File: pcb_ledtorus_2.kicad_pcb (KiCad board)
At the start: 4 copper layers, 149 x 149 mm, 279 parts, among them P1 CONN_02X04, P2 CONN_6, P3 MICRO-SD, P4 CONN_2, P5 KNUSB, P6 CONN_12, U1 STM32F46X_LQFP176, U10 TLC5955, U11 TLC5955, U12 TLC5955, U13 TLC5955, U14 TLC5955, U15 TLC5955, U2 US4881_HALL, U3 LP38691, U4 TLC5955, U5 TLC5955, U6 TLC5955, U7 TLC5955, U8 TLC5955, U9 TLC5955, X1 MA-505

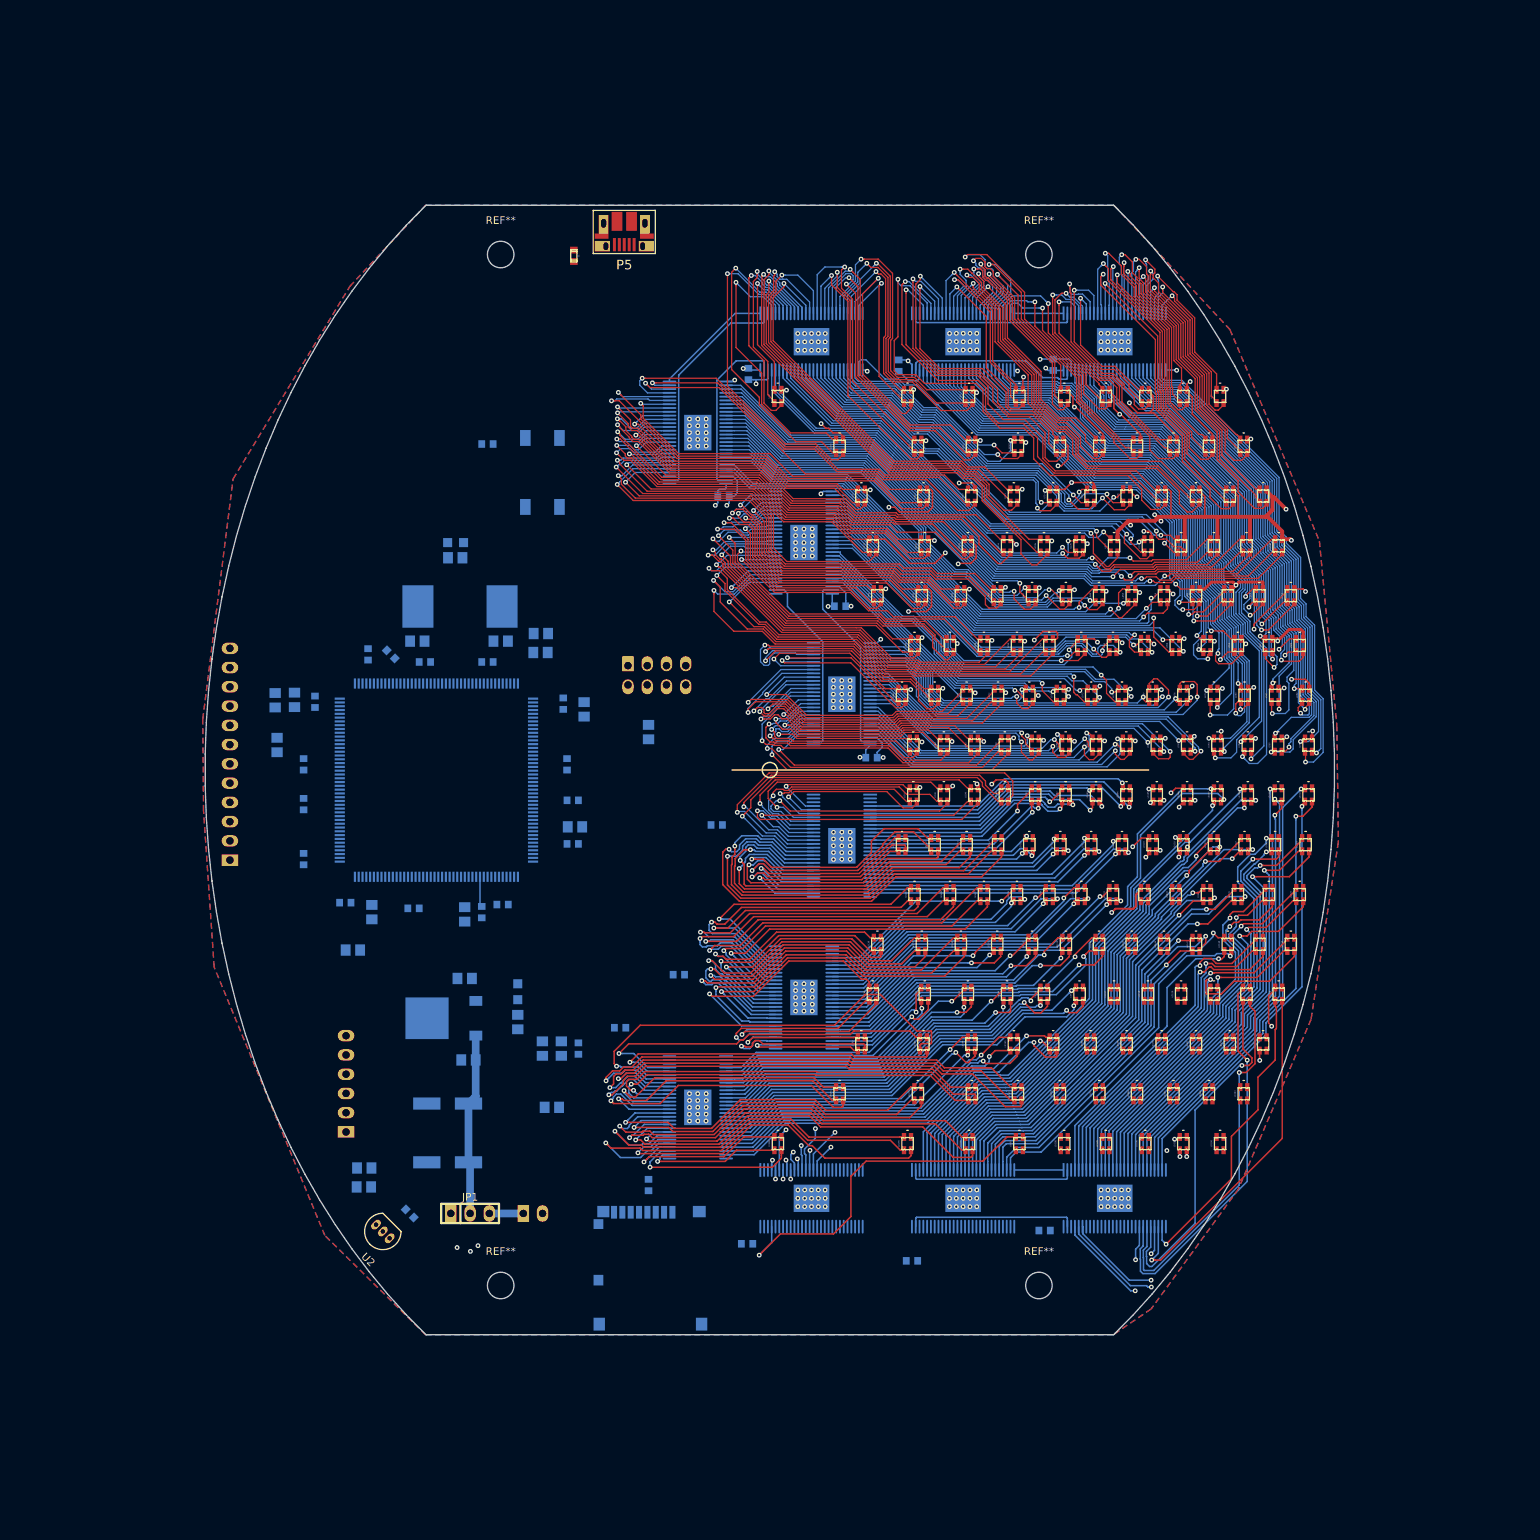
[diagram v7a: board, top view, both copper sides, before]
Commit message: Some preliminary routing of signals between TLCs and MCU.
Mostly to check that everything looks reasonably possible.
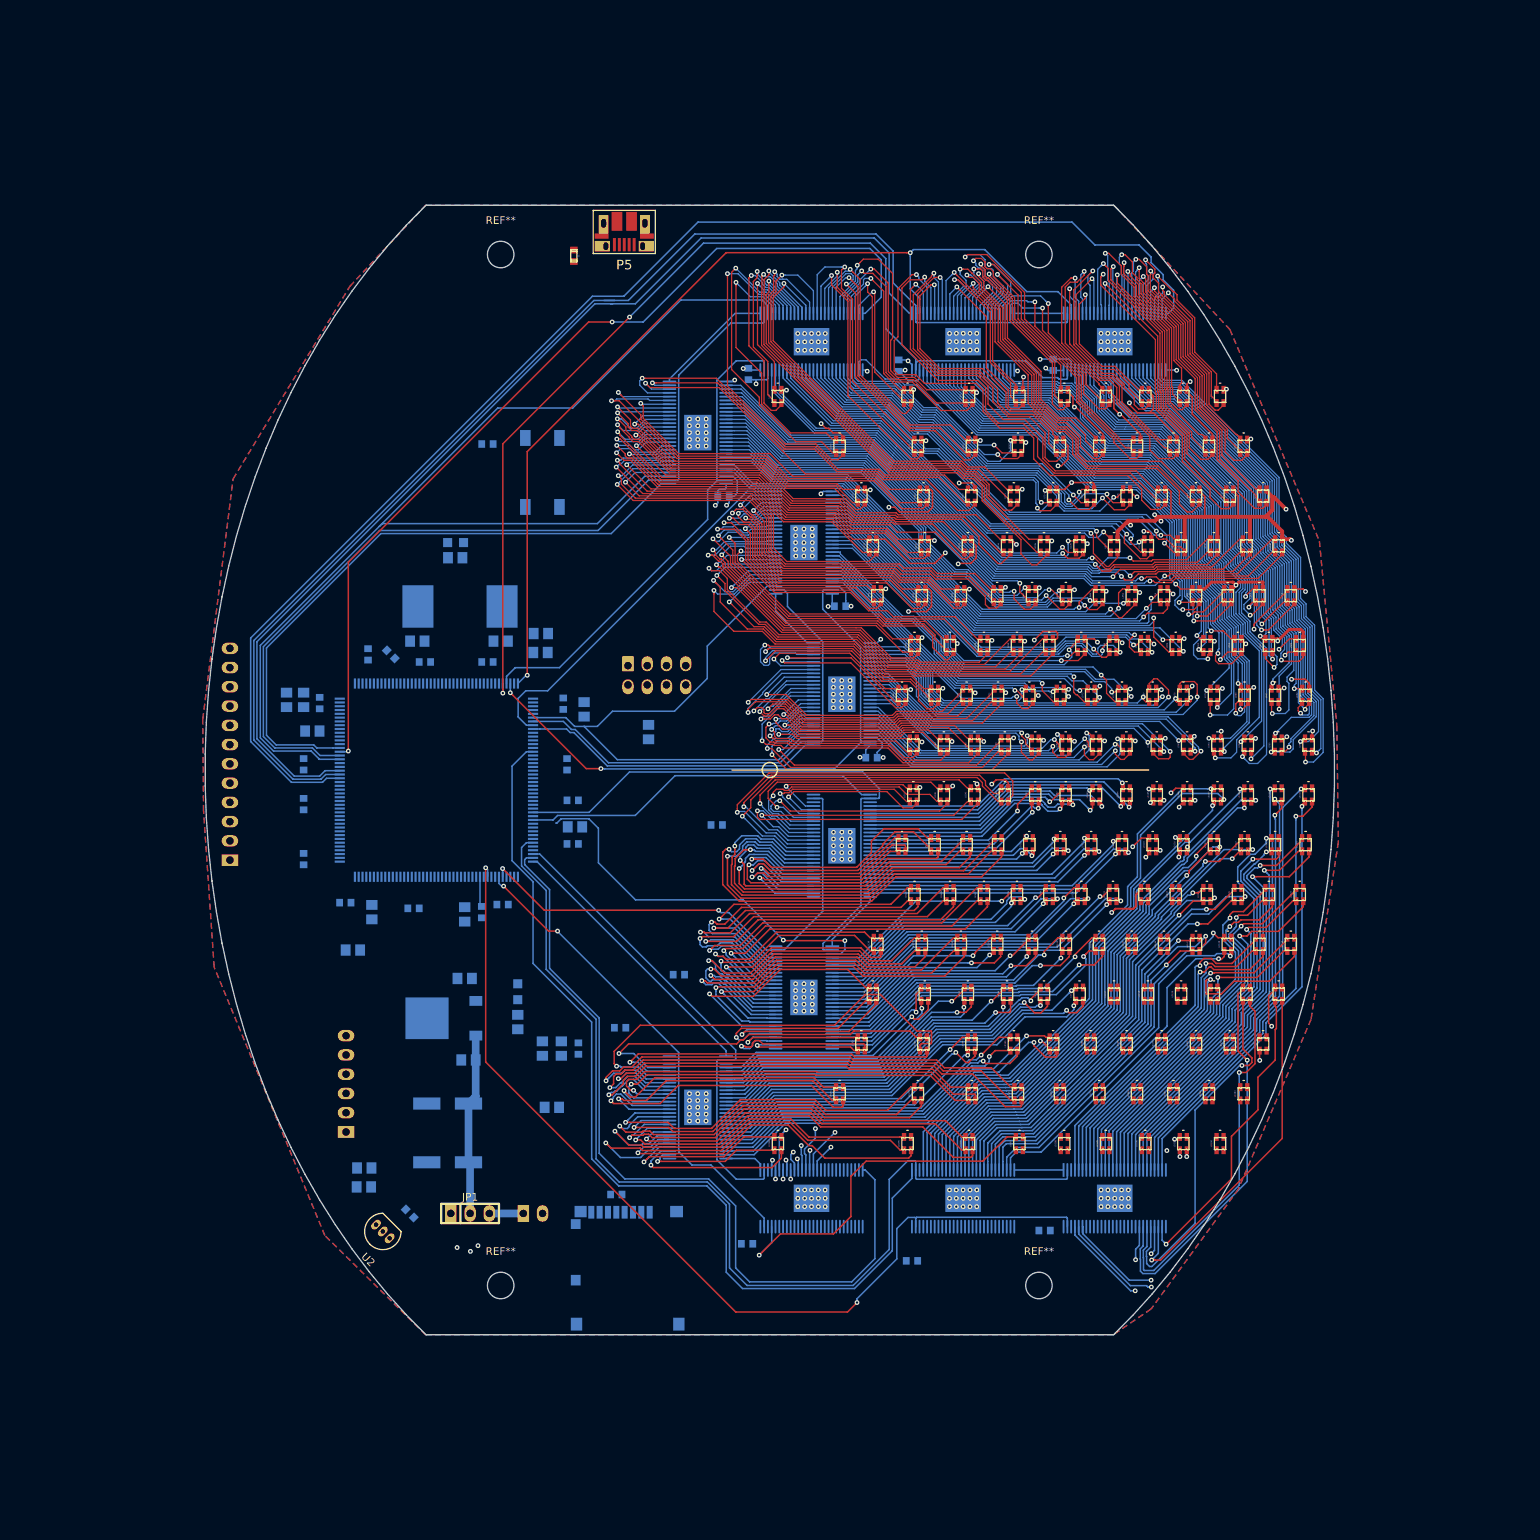
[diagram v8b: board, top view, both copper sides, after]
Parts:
- moved R10 5.00 mm to (89.7, 144.9), turned to 180 degrees
- moved C2 4.43 mm to (129.8, 206.0), turned to 0 degrees
- moved P3 3.00 mm to (131.2, 215.5)
- moved R11 1.50 mm to (86.2, 140.8)
- moved C20 1.20 mm to (88.5, 140.8)
- moved C14 0.64 mm to (90.6, 141.2)
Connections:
- U1 pad 119: /LEDs/lat2 -> Net-(U1-Pad119)
- U1 pad 155: /LEDs/sout6 -> /LEDs/sout1
- U1 pad 156: /LEDs/sclk6 -> /LEDs/sclk1
- U1 pad 157: /LEDs/sin6 -> /LEDs/sin1
- U1 pad 160: Net-(U1-Pad160) -> /LEDs/lat2
- U1 pad 161: /LEDs/sclk3 -> /LEDs/sclk2
- U1 pad 162: /LEDs/sout3 -> /LEDs/sout2
- U1 pad 163: /LEDs/sin3 -> /LEDs/sin2
- U1 pad 40: /LEDs/gsclk3 -> /LEDs/gsclk1
- U1 pad 42: /LEDs/gsclk1 -> /LEDs/gsclk3
- U1 pad 44: /LEDs/lat4 -> /LEDs/lat1
- U1 pad 50: /LEDs/lat1 -> /LEDs/lat3
- U1 pad 51: /LEDs/sclk1 -> /LEDs/sclk3
- U1 pad 52: /LEDs/sout1 -> /LEDs/sout3
- U1 pad 53: /LEDs/sin1 -> /LEDs/sin3
- U1 pad 55: /LEDs/lat3 -> Net-(U1-Pad55)
- U1 pad 59: /LEDs/sin5 -> /LEDs/sin6
- U1 pad 78: Net-(U1-Pad78) -> /LEDs/lat4
- U1 pad 83: /LEDs/sclk5 -> /LEDs/sclk6
- U1 pad 84: /LEDs/sout5 -> /LEDs/sout6
- U1 pad 86: /LEDs/sclk2 -> /LEDs/sclk5
- U1 pad 87: /LEDs/sout2 -> /LEDs/sout5
- U1 pad 88: /LEDs/sin2 -> /LEDs/sin5
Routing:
- net /LEDs/sout1: track 0.00 -> 180.6 mm
- net /LEDs/lat2: track 0.00 -> 152.0 mm
- net /LEDs/sclk1: track 22.3 -> 167.5 mm
- net /LEDs/sin1: track 0.00 -> 142.0 mm
- net /LEDs/lat1: track 0.00 -> 126.6 mm, vias 0 -> 2
- net /LEDs/sin6: track 0.00 -> 125.4 mm
- net /LEDs/sout2: track 0.00 -> 122.4 mm, vias 0 -> 2
- net /LEDs/sclk6: track 22.3 -> 136.7 mm
- net /LEDs/gsclk1: track 23.2 -> 136.0 mm, vias 0 -> 2
- net /LEDs/sout5: track 0.00 -> 106.0 mm
- net /LEDs/gsclk6: track 22.3 -> 127.5 mm, vias 0 -> 2
- net /LEDs/sclk2: track 30.3 -> 115.9 mm
- net /LEDs/sin2: track 0.00 -> 84.0 mm
- net /LEDs/lat3: track 0.00 -> 75.9 mm
- net /LEDs/sclk4: track 0.00 -> 75.6 mm
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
